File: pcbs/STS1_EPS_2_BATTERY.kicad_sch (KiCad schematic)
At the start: 23 parts, among them J9 Battery Pack, U6 TPS2420RSAT, U7 BQ29209DRBT, U9 4072

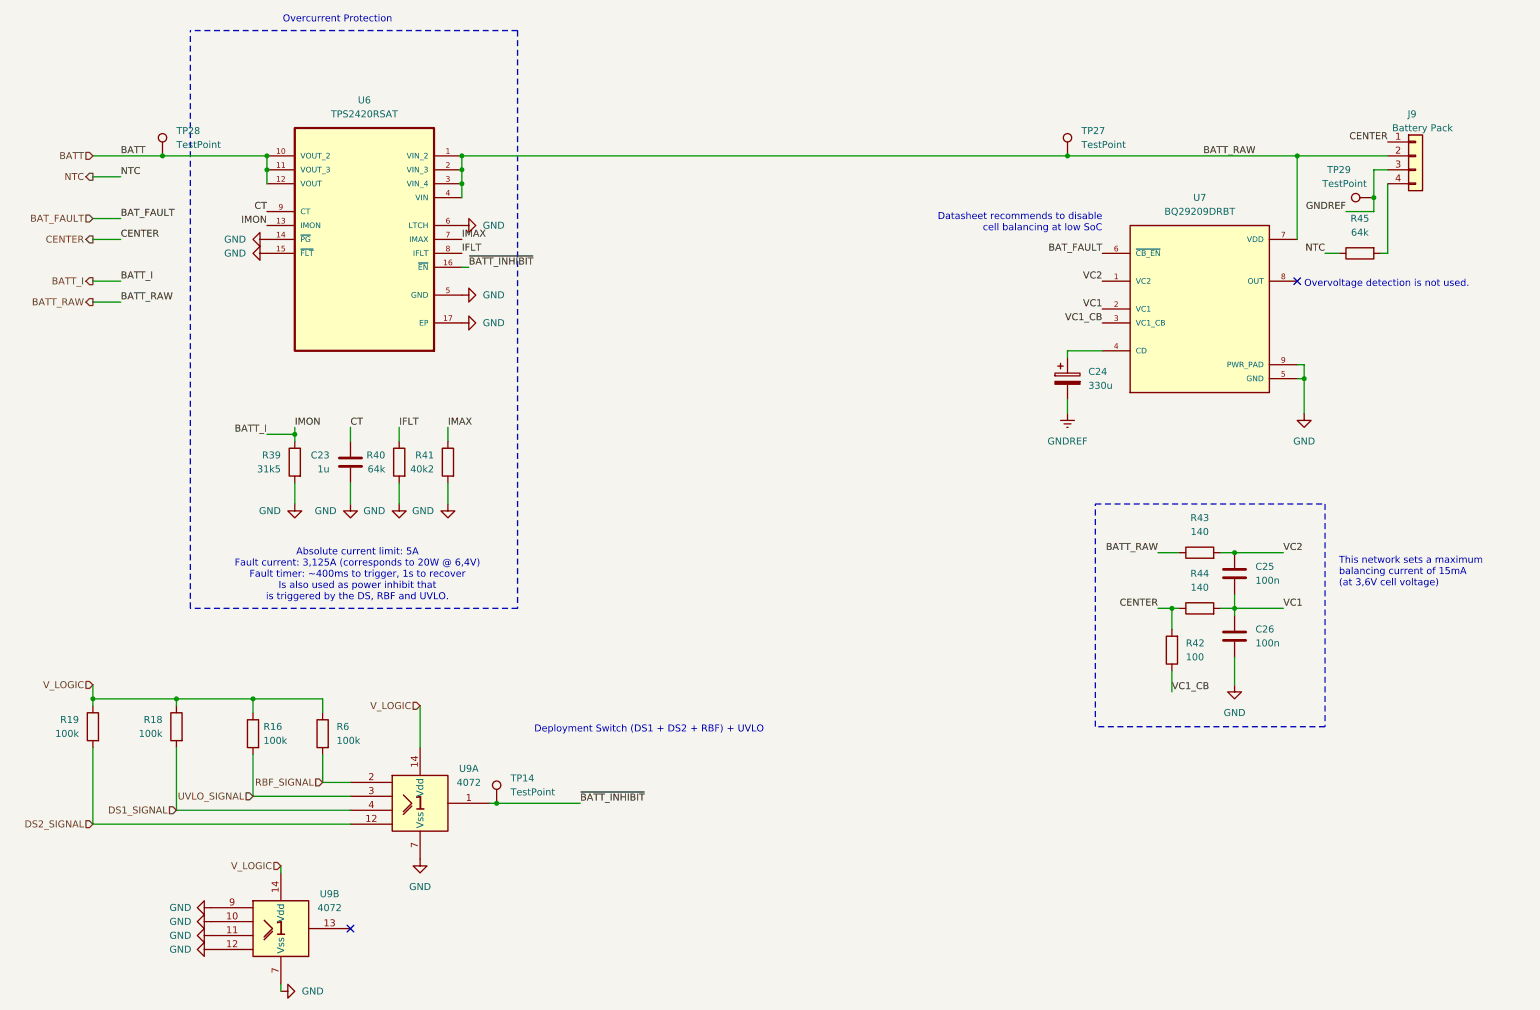
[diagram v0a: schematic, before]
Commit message: Fixed warnings and errors.
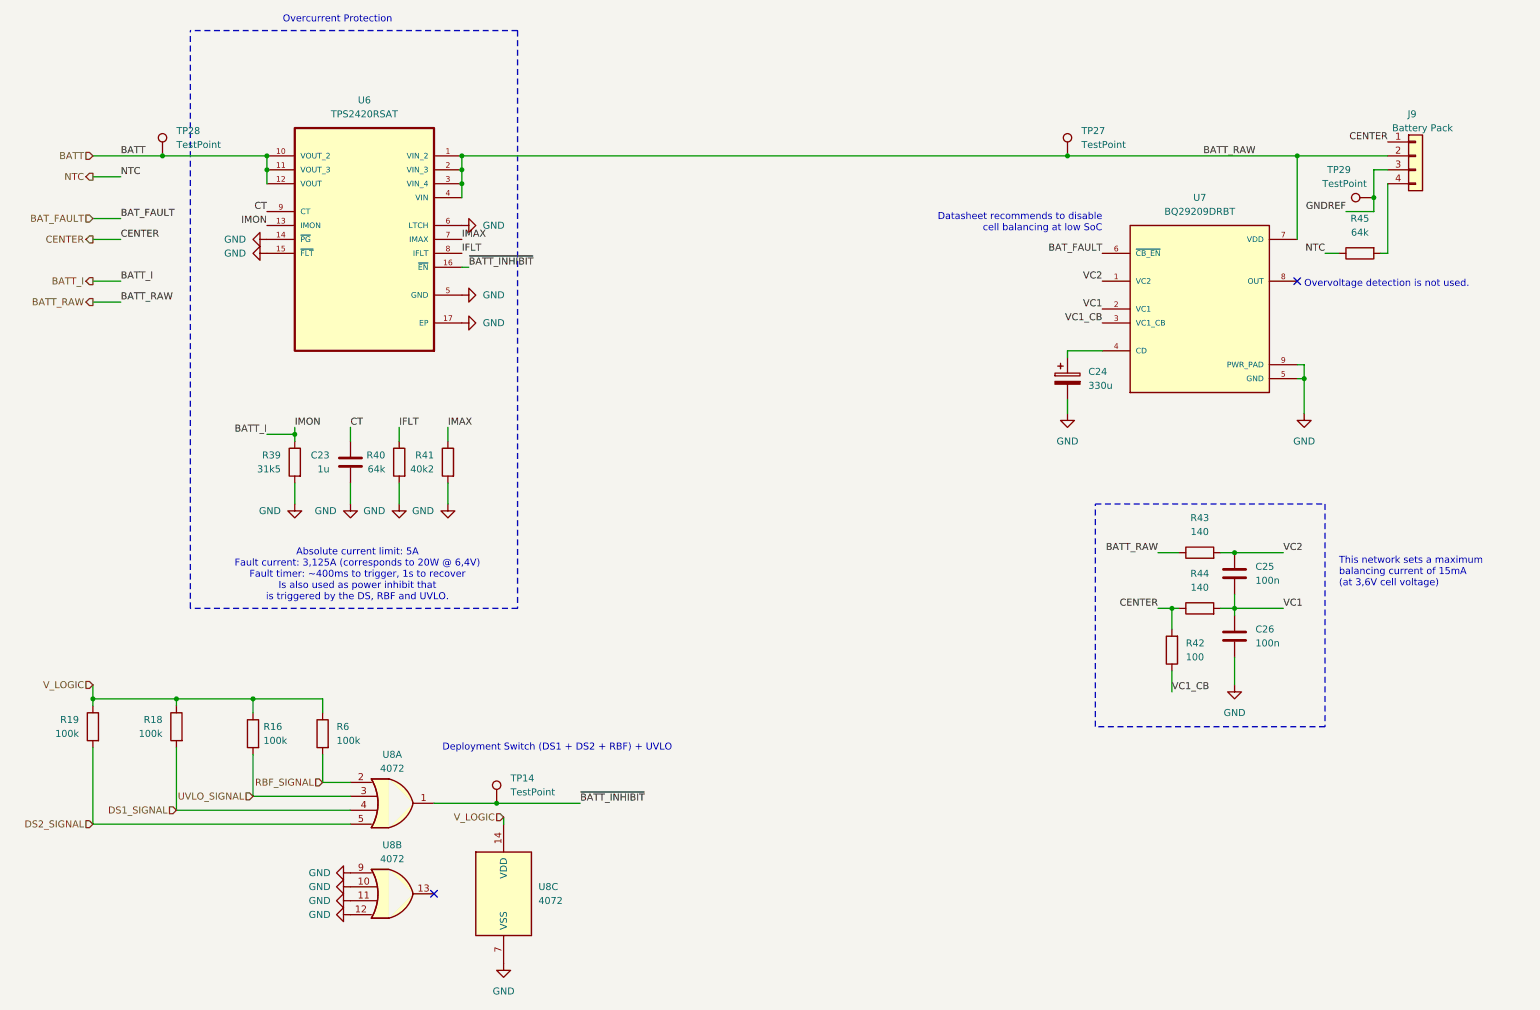
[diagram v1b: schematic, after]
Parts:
- removed U9: 4072, Package_SO:SOIC-14_3.9x8.7mm_P1.27mm, symbol 4xxx_IEEE:4072
- added U8: 4072, symbol 4xxx:4072
- U6: footprint STS_Package_DFN_QFN:QFN65P400X400X100-17N -> Package_DFN_QFN:VQFN-16-1EP_3x3mm_P0.5mm_EP1.45x1.45mm_ThermalVias
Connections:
- net DS1_SIGNAL: now also U8.4
- net DS2_SIGNAL: now also U8.5
- net GND: now also C24.2, U8.10, U8.11, U8.12, U8.7 (VSS), U8.9
- net GNDREF: no longer C24.2
- net RBF_SIGNAL: now also U8.2
- net UVLO_SIGNAL: now also U8.3
- net V_LOGIC: now also U8.14 (VDD)
- net ~{BATT_INHIBIT}: now also U8.1

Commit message: Intermediate commit.
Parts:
- U8: footprint (none) -> Package_SO:SOIC-14_3.9x8.7mm_P1.27mm
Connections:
- net GNDREF is gone; now on net GND: J9.3 (Pin_3), TP29.1
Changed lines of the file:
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@@
 	)
 	(junction
+		(at 260.35 44.45)
+		(diameter 0)
+		(color 0 0 0 0)
+	)
+	(junction
 		(at 93.98 46.99)
 		(diameter 0)
@@
 	)
 	(junction
-		(at 260.35 49.53)
-		(diameter 0)
-		(color 0 0 0 0)
-	)
-	(junction
 		(at 247.65 82.55)
 		(diameter 0)
@@
 	(wire
 		(pts
-			(xy 260.35 52.07) (xy 260.35 49.53)
-		)
-		(stroke
-			(width 0)
-			(type default)
-		)
-	)
-	(wire
-		(pts
 			(xy 68.58 143.51) (xy 68.58 140.97)
 		)
@@
 	(wire
 		(pts
-			(xy 255.27 52.07) (xy 260.35 52.07)
-		)
-		(stroke
-			(width 0)
-			(type default)
-		)
-	)
-	(wire
-		(pts
 			(xy 234.95 114.3) (xy 243.84 114.3)
 		)
@@
 		)
 	)
-	(label "GNDREF"
-		(at 255.27 52.07 180)
-		(fields_autoplaced yes)
-		(effects
-			(font
-				(size 1.27 1.27)
-			)
-			(justify right bottom)
-		)
-	)
 	(label "IMON"
 		(at 63.5 91.44 0)
@@
 			)
 		)
-		(property "Footprint" ""
+		(property "Footprint" "Package_SO:SOIC-14_3.9x8.7mm_P1.27mm"
 			(at 81.28 160.02 0)
 			(effects
@@
 			)
 		)
-		(property "Footprint" ""
+		(property "Footprint" "Package_SO:SOIC-14_3.9x8.7mm_P1.27mm"
 			(at 101.6 176.53 0)
 			(effects
@@
 	)
 	(symbol
+		(lib_id "power:GND")
+		(at 260.35 44.45 270)
+		(mirror x)
+		(unit 1)
+		(exclude_from_sim no)
+		(in_bom yes)
+		(on_board yes)
+		(dnp no)
+		(fields_autoplaced yes)
+		(property "Reference" "#PWR0100"
+			(at 254 44.45 0)
+			(effects
+				(font
+					(size 1.27 1.27)
+				)
+				(hide yes)
+			)
+		)
+		(property "Value" "GND"
+			(at 256.54 44.4499 90)
+			(effects
+				(font
+					(size 1.27 1.27)
+				)
+				(justify right)
+			)
+		)
+		(property "Footprint" ""
+			(at 260.35 44.45 0)
+			(effects
+				(font
+					(size 1.27 1.27)
+				)
+				(hide yes)
+			)
+		)
+		(property "Datasheet" ""
+			(at 260.35 44.45 0)
+			(effects
+				(font
+					(size 1.27 1.27)
+				)
+				(hide yes)
+			)
+		)
+		(property "Description" "Power symbol creates a global label with name \"GND\" , ground"
+			(at 260.35 44.45 0)
+			(effects
+				(font
+					(size 1.27 1.27)
+				)
+				(hide yes)
+			)
+		)
+		(pin "1"
+		)
+		(instances
+			(project "STS1_EPS_2"
+				(path "/38c03ff7-ea47-4d00-b37d-ddcaa7d87722/75dca64b-8858-4c1f-8340-a846cd3da1d0"
+					(reference "#PWR0100")
+					(unit 1)
+				)
+			)
+		)
+	)
+	(symbol
 		(lib_id "Connector:TestPoint")
 		(at 260.35 49.53 90)
@@
 			)
 		)
-		(property "Footprint" ""
+		(property "Footprint" "Package_SO:SOIC-14_3.9x8.7mm_P1.27mm"
 			(at 81.28 176.53 0)
 			(effects

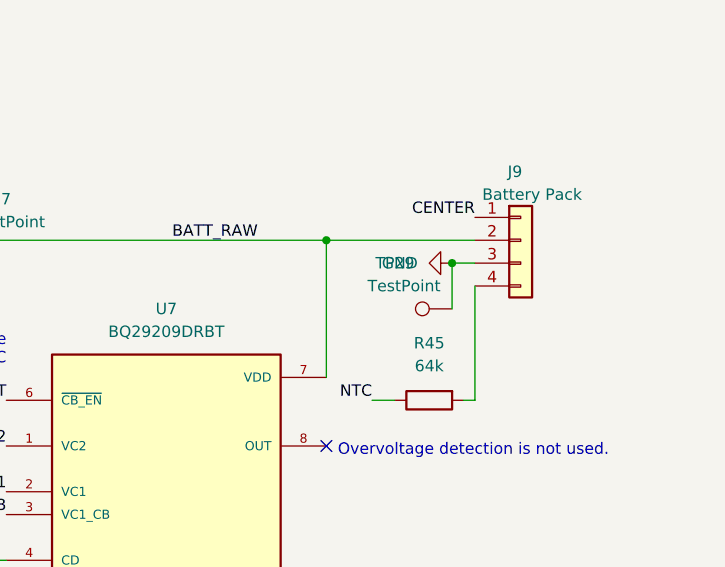
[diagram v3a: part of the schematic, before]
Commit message: Reduced both EPS PCBs down to 0 DRC errors.
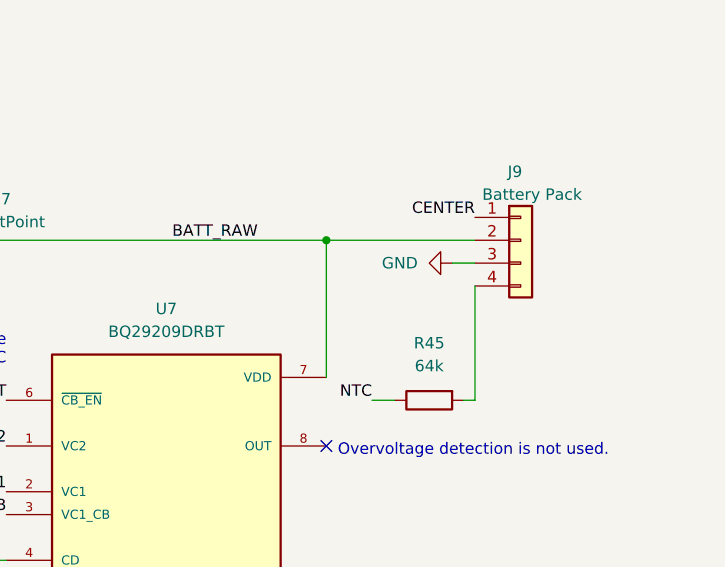
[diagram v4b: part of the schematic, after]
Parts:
- removed TP29: TestPoint, TestPoint:TestPoint_THTPad_D1.0mm_Drill0.5mm, symbol Connector:TestPoint
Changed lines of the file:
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@@
 	)
 	(junction
-		(at 260.35 44.45)
-		(diameter 0)
-		(color 0 0 0 0)
-	)
-	(junction
 		(at 93.98 46.99)
 		(diameter 0)
@@
 	(wire
 		(pts
-			(xy 260.35 49.53) (xy 260.35 44.45)
-		)
-		(stroke
-			(width 0)
-			(type default)
-		)
-	)
-	(wire
-		(pts
 			(xy 204.47 41.91) (xy 246.38 41.91)
 		)
@@
 					(unit 1)
 				)
-			)
-		)
-	)
-	(symbol
-		(lib_id "Connector:TestPoint")
-		(at 260.35 49.53 90)
-		(unit 1)
-		(exclude_from_sim no)
-		(in_bom yes)
-		(on_board yes)
-		(dnp no)
-		(property "Reference" "TP29"
-			(at 254 44.45 90)
-			(effects
-				(font
-					(size 1.27 1.27)
-				)
-			)
-		)
-		(property "Value" "TestPoint"
-			(at 255.016 46.99 90)
-			(effects
-				(font
-					(size 1.27 1.27)
-				)
-			)
-		)
-		(property "Footprint" "TestPoint:TestPoint_THTPad_D1.0mm_Drill0.5mm"
-			(at 260.35 44.45 0)
-			(effects
-				(font
-					(size 1.27 1.27)
-				)
-				(hide yes)
-			)
-		)
-		(property "Datasheet" "~"
-			(at 260.35 44.45 0)
-			(effects
-				(font
-					(size 1.27 1.27)
-				)
-				(hide yes)
-			)
-		)
-		(property "Description" ""
-			(at 260.35 49.53 0)
-			(effects
-				(font
-					(size 1.27 1.27)
-				)
-				(hide yes)
-			)
-		)
-		(pin "1"
-		)
-		(instances
-			(project "STS1_EPS_2"
-				(path "/38c03ff7-ea47-4d00-b37d-ddcaa7d87722/75dca64b-8858-4c1f-8340-a846cd3da1d0"
-					(reference "TP29")
-					(unit 1)
-				)

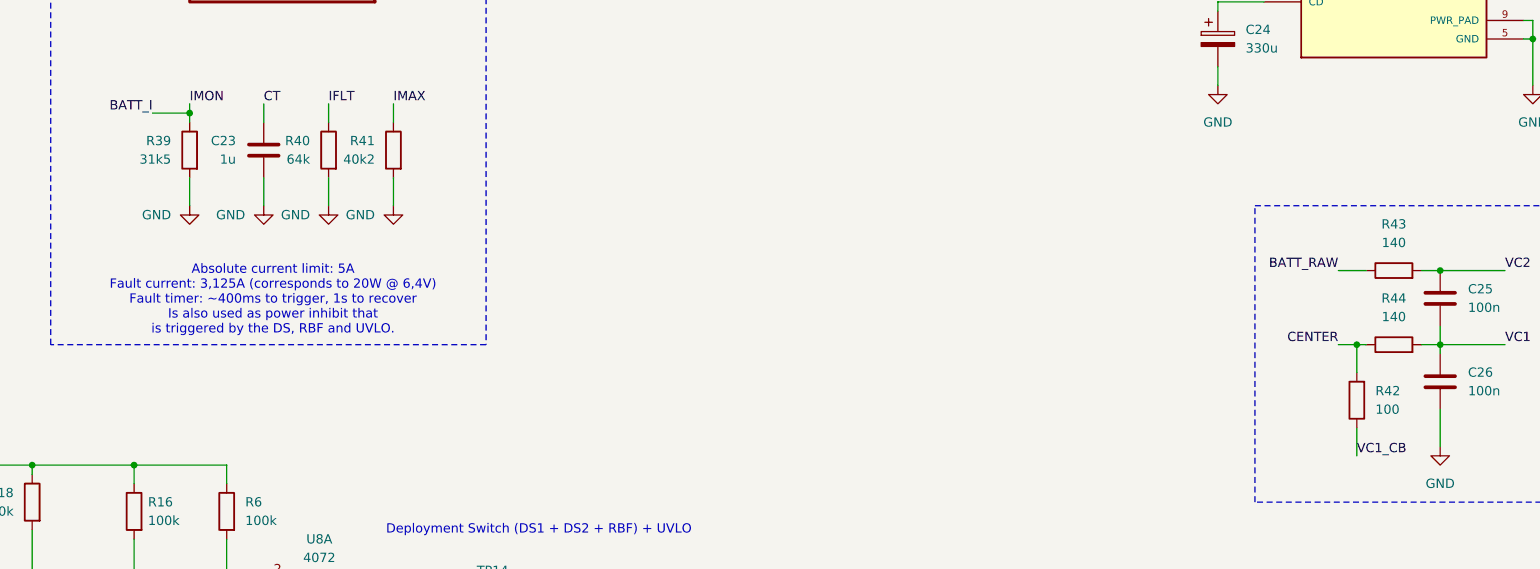
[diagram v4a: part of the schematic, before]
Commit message: Modified some resistor values slightly, so that they fall in common resistor series.
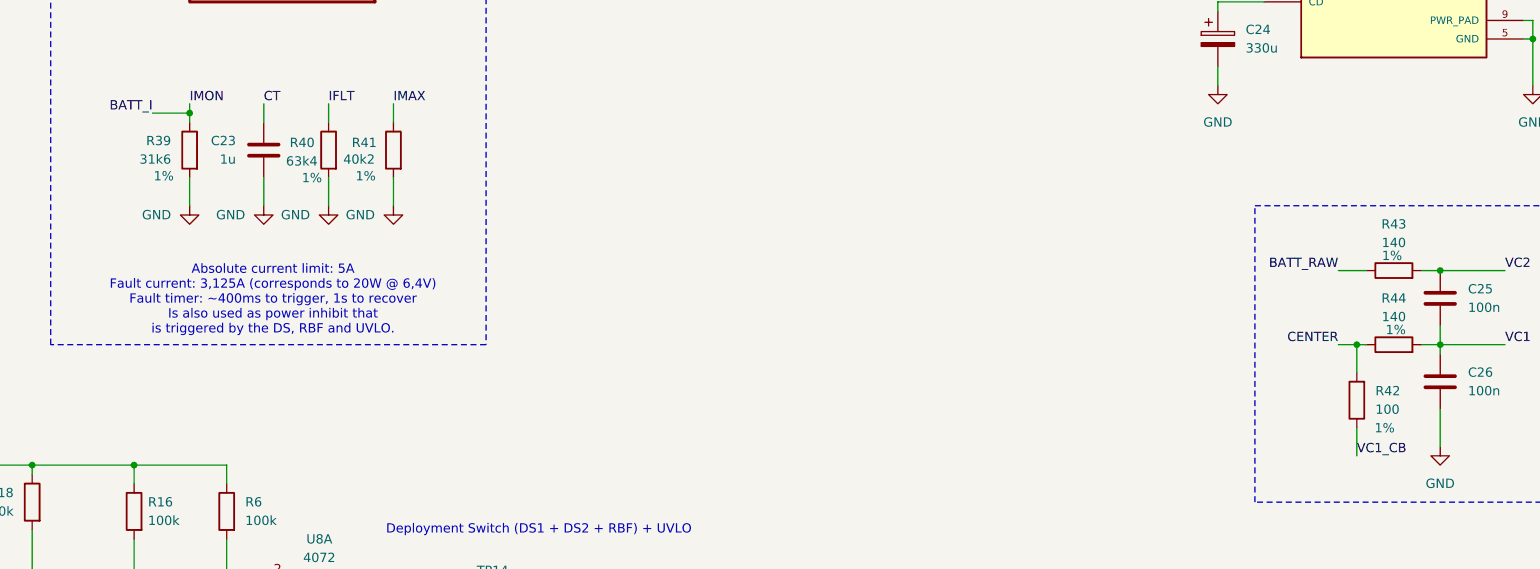
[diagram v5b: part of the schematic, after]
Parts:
- R39: value 31k5 -> 31k6; Tolerance (none) -> 1%
- R40: value 64k -> 63k4; Tolernace (none) -> 1%
- R41, R42, R43, R44: Tolerance (none) -> 1%
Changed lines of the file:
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@@
 		(on_board yes)
 		(dnp no)
-		(fields_autoplaced yes)
 		(property "Reference" "R41"
-			(at 88.9 96.5199 0)
+			(at 89.154 96.774 0)
 			(effects
 				(font
@@
 				)
 				(hide yes)
+			)
+		)
+		(property "Tolerance" "1%"
+			(at 87.63 101.346 0)
+			(effects
+				(font
+					(size 1.27 1.27)
+				)
 			)
 		)
@@
 		(on_board yes)
 		(dnp no)
-		(fields_autoplaced yes)
 		(property "Reference" "R39"
 			(at 60.96 96.5199 0)
@@
 			)
 		)
-		(property "Value" "31k5"
+		(property "Value" "31k6"
 			(at 60.96 99.0599 0)
 			(effects
@@
 				)
 				(hide yes)
+			)
+		)
+		(property "Tolerance" "1%"
+			(at 59.944 101.346 0)
+			(effects
+				(font
+					(size 1.27 1.27)
+				)
 			)
 		)
@@
 		(on_board yes)
 		(dnp no)
-		(fields_autoplaced yes)
 		(property "Reference" "R42"
 			(at 226.06 130.8099 0)
@@
 				)
 				(hide yes)
+			)
+		)
+		(property "Tolerance" "1%"
+			(at 227.33 135.89 0)
+			(effects
+				(font
+					(size 1.27 1.27)
+				)
 			)
 		)
@@
 		(on_board yes)
 		(dnp no)
-		(fields_autoplaced yes)
 		(property "Reference" "R43"
 			(at 228.6 107.95 90)
@@
 				)
 				(hide yes)
+			)
+		)
+		(property "Tolerance" "1%"
+			(at 228.346 112.268 90)
+			(effects
+				(font
+					(size 1.27 1.27)
+				)
 			)
 		)
@@
 		(on_board yes)
 		(dnp no)
-		(fields_autoplaced yes)
 		(property "Reference" "R40"
-			(at 80.01 96.5199 0)
-			(effects
-				(font
-					(size 1.27 1.27)
-				)
-				(justify left)
-			)
-		)
-		(property "Value" "64k"
-			(at 80.01 99.0599 0)
-			(effects
-				(font
-					(size 1.27 1.27)
-				)
-				(justify left)
+			(at 77.216 96.774 0)
+			(effects
+				(font
+					(size 1.27 1.27)
+				)
+				(justify right)
+			)
+		)
+		(property "Value" "63k4"
+			(at 76.708 99.314 0)
+			(effects
+				(font
+					(size 1.27 1.27)
+				)
+				(justify right)
 			)
 		)
@@
 			)
 		)
+		(property "Tolernace" "1%"
+			(at 80.264 101.6 0)
+			(effects
+				(font
+					(size 1.27 1.27)
+				)
+			)
+		)
 		(pin "1"
 		)
@@
 		(on_board yes)
 		(dnp no)
-		(fields_autoplaced yes)
 		(property "Reference" "R44"
 			(at 228.6 118.11 90)
@@
 			)
 		)
+		(property "Tolerance" "1%"
+			(at 228.854 122.428 90)
+			(effects
+				(font
+					(size 1.27 1.27)
+				)
+			)
+		)

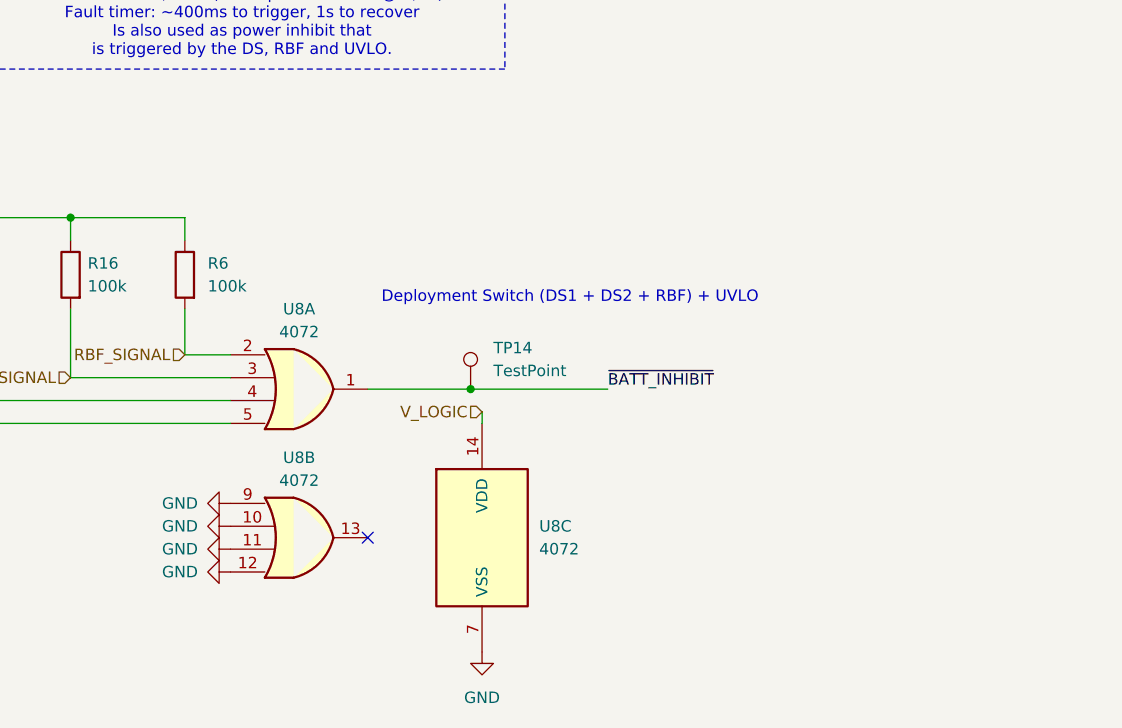
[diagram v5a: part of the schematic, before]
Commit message: Logic gates now use ISO symbols consistently.
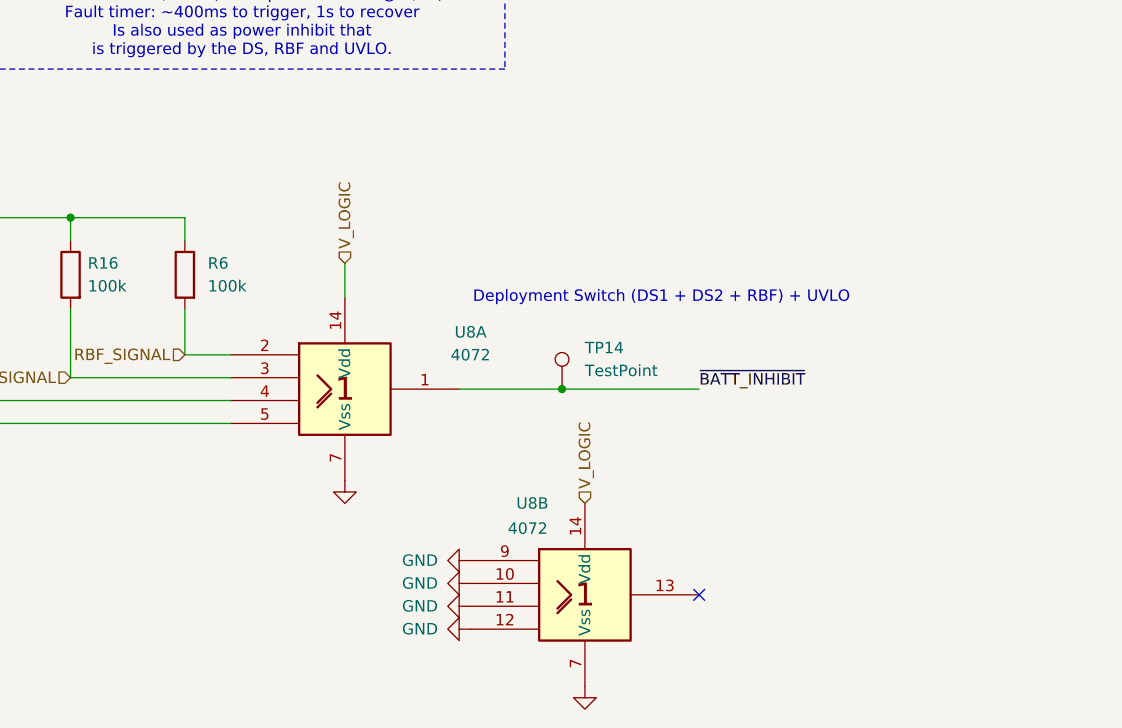
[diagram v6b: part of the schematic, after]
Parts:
- removed unit 3 of U8
- U8: symbol 4xxx:4072 -> 4xxx_IEEE:4072
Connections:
- net GND: now also U8.7 (Vss), U8.7 (Vss)
- net V_LOGIC: now also U8.14 (Vdd), U8.14 (Vdd)
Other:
- moved on the sheet: TP14
